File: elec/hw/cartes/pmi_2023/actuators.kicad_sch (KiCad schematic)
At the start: 43 parts, among them J1 con_servo, J2 con_servo, J3 con_servo, J4 con_servo, U23 PCA9685PW, U24 SN74LVC1T45DBV, U25 SN74LVC1T45DBV, U26 SN74LVC1T45DBV, U27 SN74LVC1T45DBV

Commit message: PAMI 2023: update jlc part number
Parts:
- R62, R63, R64: JLCPCB C2991540 -> C21190
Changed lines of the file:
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@@
 			)
 		)
-		(property "JLCPCB" "C2991540"
+		(property "JLCPCB" "C21190"
 			(at 166.37 33.02 0)
 			(effects
@@
 			)
 		)
-		(property "JLCPCB" "C2991540"
+		(property "JLCPCB" "C21190"
 			(at 149.86 33.02 0)
 			(effects
@@
 			)
 		)
-		(property "JLCPCB" "C2991540"
+		(property "JLCPCB" "C21190"
 			(at 137.16 33.02 0)
 			(effects

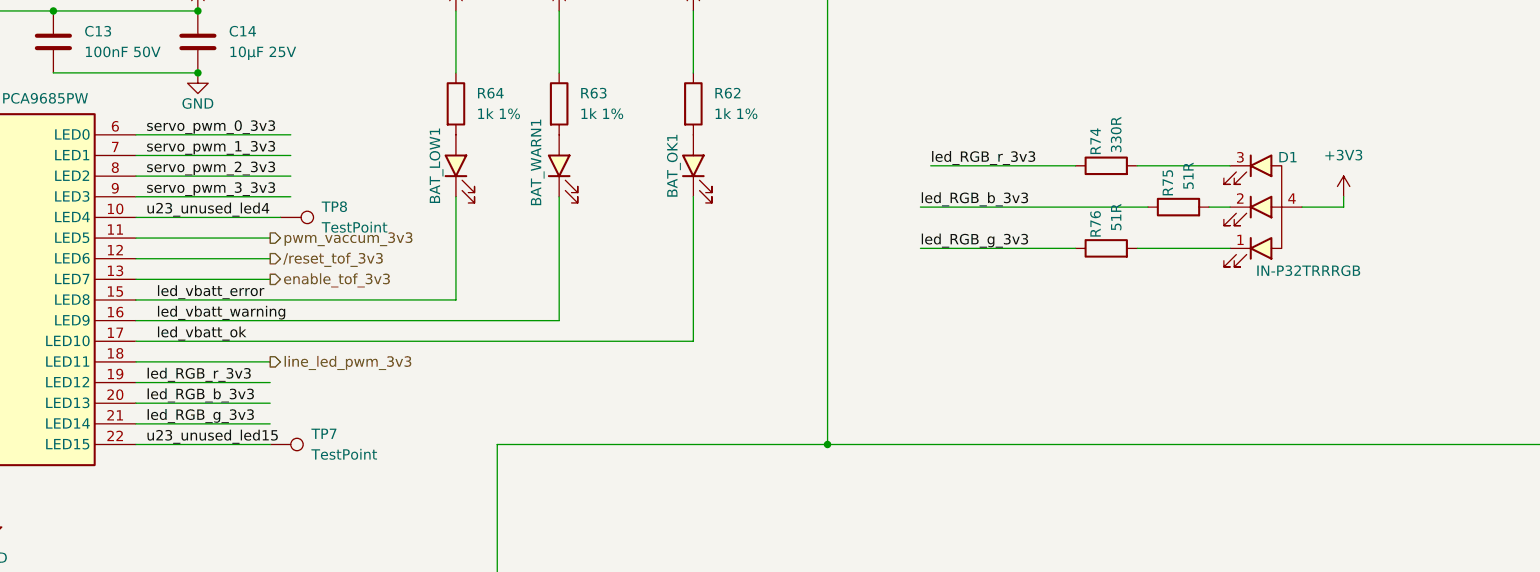
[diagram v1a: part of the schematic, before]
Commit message: GP2S60B replaced by ITR1204SR10A, RGB LED replaced by NH-B2020RGBA
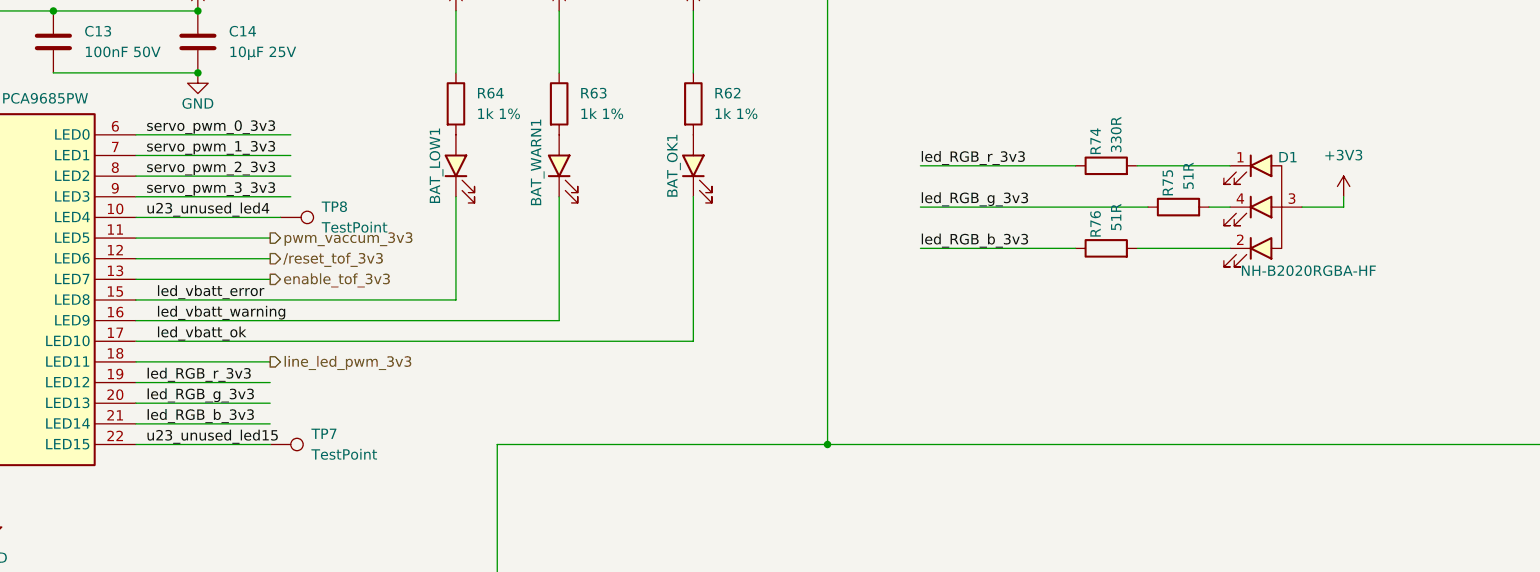
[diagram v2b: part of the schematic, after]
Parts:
- D1: value IN-P32TRRRGB -> NH-B2020RGBA-HF; footprint cocotter_diodes:3528_PLCC-Reverse_mount -> cocotter_diodes:NH-B2020RGBA-HF; symbol cocotter_diodes:IN-P32TRRRGB -> cocotter_diodes:NH-B2020RGBA-HF; JLCPCB C7288909 -> C2874116
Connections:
- net +3V3: now also D1.3 (COM); no longer D1.4 (COM)
- net led_RGB_b_3v3: now also R76.1, U23.21 (LED14); no longer R75.1, U23.20 (LED13)
- net led_RGB_g_3v3: now also R75.1, U23.20 (LED13); no longer R76.1, U23.21 (LED14)
- net at R75.2: now also D1.4 (C_GREEN); no longer D1.2 (C_GREEN)
- net at R76.2: now also D1.2 (C_BLUE); no longer D1.1 (C_BLUE)
- net at R74.2: now also D1.1 (C_RED); no longer D1.3 (C_RED)
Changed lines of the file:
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@@
 	(wire
 		(pts
-			(xy 195.58 40.64) (xy 213.36 40.64)
+			(xy 194.31 40.64) (xy 213.36 40.64)
 		)
 		(stroke
@@
 		)
 	)
-	(label "led_RGB_b_3v3"
+	(label "led_RGB_g_3v3"
 		(at 99.06 69.85 0)
 		(fields_autoplaced yes)
@@
 		)
 	)
-	(label "led_RGB_b_3v3"
+	(label "led_RGB_g_3v3"
 		(at 194.31 45.72 0)
 		(fields_autoplaced yes)
@@
 		)
 	)
-	(label "led_RGB_g_3v3"
+	(label "led_RGB_b_3v3"
 		(at 194.31 50.8 0)
 		(fields_autoplaced yes)
@@
 		)
 	)
-	(label "led_RGB_g_3v3"
+	(label "led_RGB_b_3v3"
 		(at 99.06 72.39 0)
 		(fields_autoplaced yes)
@@
 	)
 	(label "led_RGB_r_3v3"
-		(at 195.58 40.64 0)
+		(at 194.31 40.64 0)
 		(fields_autoplaced yes)
 		(effects
@@
 	)
 	(symbol
-		(lib_id "cocotter_diodes:IN-P32TRRRGB")
+		(lib_id "cocotter_diodes:NH-B2020RGBA-HF")
 		(at 237.49 45.72 0)
 		(unit 1)
@@
 			)
 		)
-		(property "Value" "IN-P32TRRRGB"
+		(property "Value" "NH-B2020RGBA-HF"
 			(at 242.062 53.594 0)
 			(effects
@@
 			)
 		)
-		(property "Footprint" "cocotter_diodes:3528_PLCC-Reverse_mount"
+		(property "Footprint" "cocotter_diodes:NH-B2020RGBA-HF"
 			(at 237.49 45.72 0)
 			(effects
@@
 			)
 		)
-		(property "Description" "RGB LED, reverse mount"
+		(property "Description" "RGB LED 2.1mm x 2.1mm"
 			(at 237.49 45.72 0)
 			(effects
@@
 			)
 		)
-		(property "JLCPCB" "C7288909"
+		(property "JLCPCB" "C2874116"
 			(at 237.49 45.72 0)
 			(effects

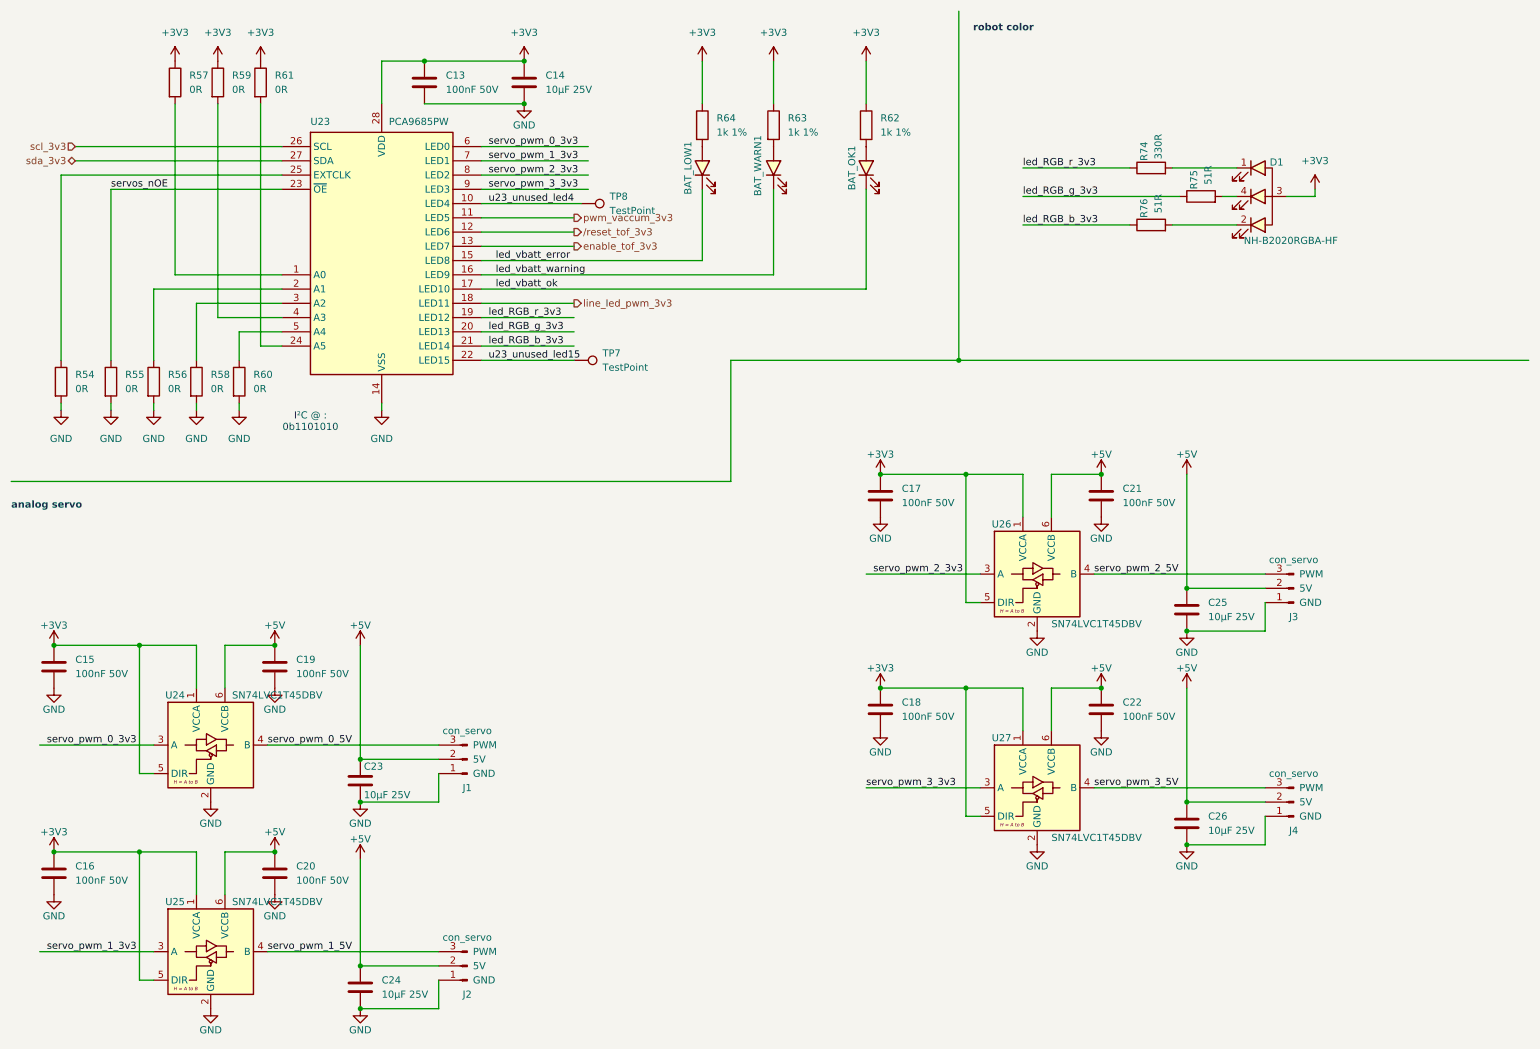
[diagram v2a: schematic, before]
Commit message: pmi_tof_sensor : last commit before tmf8821 deletion
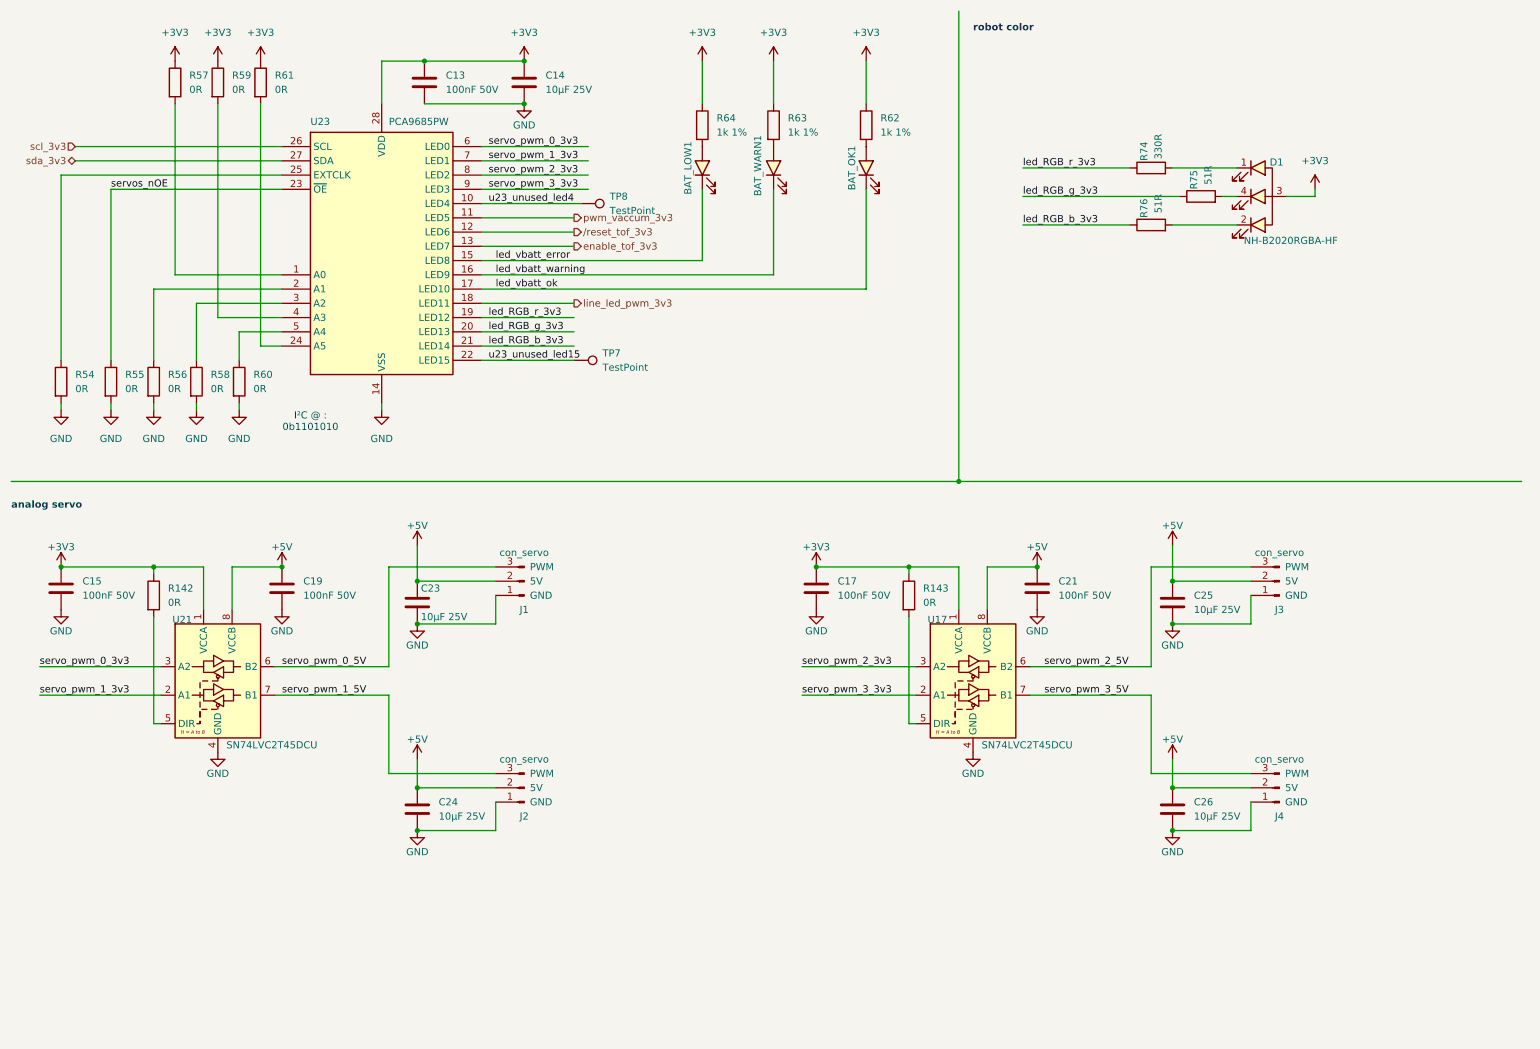
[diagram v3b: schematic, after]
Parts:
- removed C16, C18, C20, C22: 100nF 50V, cocotter_capacitors:C_0603_1608Metric, symbol cocotter_capacitors:C_100nF_50V_0603
- removed U24, U25, U26, U27: SN74LVC1T45DBV, Package_TO_SOT_SMD:SOT-23-6, symbol cocotter_ic:SN74LVC1T45DBV
- added R142, R143: 0R, cocotter_resistor:r0603_reflow, symbol cocotter_resistors:R_0R_0603
- added U17, U21: SN74LVC2T45DCU, cocotter_ic:VSSOP-8-DCU, symbol cocotter_ic:SN74LVC2T45DCU
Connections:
- net +3V3: now also R142.1, R143.1, U17.1 (VCCA), U21.1 (VCCA)
- net +5V: now also U17.8 (VCCB), U21.8 (VCCB)
- net GND: now also U17.4 (GND), U21.4 (GND)
- net servo_pwm_0_3v3: now also U21.3 (A2)
- net servo_pwm_0_5V: now also U21.6 (B2)
- net servo_pwm_1_3v3: now also U21.2 (A1)
- net servo_pwm_1_5V: now also U21.7 (B1)
- net servo_pwm_2_3v3: now also U17.3 (A2)
- net servo_pwm_2_5V: now also U17.6 (B2)
- net servo_pwm_3_3v3: now also U17.2 (A1)
- net servo_pwm_3_5V: now also U17.7 (B1)
- new net: R143.2, U17.5 (DIR)
- new net: R142.2, U21.5 (DIR)
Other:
- moved on the sheet: C15, C17, C19, C21, C23, C24, C25, C26, J1, J2, J3, J4

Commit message: XRA1200 replaced by TCA6408
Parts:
- BAT_LOW1: JLCPCB C2286 -> (none)
- BAT_OK1: JLCPCB C2290 -> (none); JLCPCB Part # (none) -> C2290
- BAT_WARN1: JLCPCB C2296 -> (none)
- C13, C15, C17, C19, C21: JLCPCB C14663 -> (none); JLCPCB Part # (none) -> C14663
- C14, C23, C24, C25, C26: JLCPCB C15850 -> (none); JLCPCB Part # (none) -> C15850
- D1: JLCPCB C2874116 -> (none); JLCPCB Part # (none) -> C2874116
- J1, J2, J3, J4: JLCPCB C2932698 -> (none); JLCPCB Part # (none) -> C2932698
- R142, R143, R54, R55, R56, R57, R58, R59, R60, R61: JLCPCB C431718 -> (none); JLCPCB Part # (none) -> C431718
- R62, R63, R64: JLCPCB C21190 -> (none); JLCPCB Part # (none) -> C2991540
- R74: JLCPCB C23138 -> (none); JLCPCB Part # (none) -> C23138
- R75, R76: JLCPCB C23197 -> (none); JLCPCB Part # (none) -> C23197
- U23: JLCPCB C2678753 -> (none); JLCPCB Part # (none) -> C2678753
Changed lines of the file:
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@@
 			)
 		)
-		(property "JLCPCB" "C2678753"
+		(property "JLCPCB Part #" "C2678753"
 			(at 80.01 54.61 0)
 			(effects
@@
 			)
 		)
-		(property "JLCPCB" "C431718"
+		(property "JLCPCB Part #" "C431718"
 			(at 173.99 116.84 0)
 			(effects
@@
 			)
 		)
-		(property "JLCPCB" "C14663"
+		(property "JLCPCB Part #" "C14663"
 			(at 62.23 115.57 0)
 			(effects
@@
 			)
 		)
-		(property "JLCPCB" "C15850"
+		(property "JLCPCB Part #" "C15850"
 			(at 86.36 118.11 0)
 			(effects
@@
 			)
 		)
-		(property "JLCPCB" "C15850"
+		(property "JLCPCB Part #" "C15850"
 			(at 220.98 154.94 0)
 			(effects
@@
 			)
 		)
-		(property "JLCPCB" "C21190"
+		(property "JLCPCB Part #" "C2991540"
 			(at 166.37 33.02 0)
 			(effects
@@
 			)
 		)
-		(property "JLCPCB" "C431718"
+		(property "JLCPCB Part #" "C431718"
 			(at 39.37 78.74 0)
 			(effects
@@
 			)
 		)
-		(property "JLCPCB" "C431718"
+		(property "JLCPCB Part #" "C431718"
 			(at 22.86 78.74 0)
 			(effects
@@
 			)
 		)
-		(property "JLCPCB" "C431718"
+		(property "JLCPCB Part #" "C431718"
 			(at 39.37 116.84 0)
 			(effects
@@
 			)
 		)
-		(property "JLCPCB" "C431718"
+		(property "JLCPCB Part #" "C431718"
 			(at 31.75 78.74 0)
 			(effects
@@
 			)
 		)
-		(property "JLCPCB" "C2932698"
+		(property "JLCPCB Part #" "C2932698"
 			(at 240.03 114.3 0)
 			(effects
@@
 			)
 		)
-		(property "JLCPCB" ""
+		(property "JLCPCB Part #" ""
 			(at 185.42 134.62 0)
 			(effects
@@
 			)
 		)
-		(property "JLCPCB" "C23197"
+		(property "JLCPCB Part #" "C23197"
 			(at 226.06 45.72 0)
 			(effects
@@
 			)
 		)
-		(property "JLCPCB" "C23197"
+		(property "JLCPCB Part #" "C23197"
 			(at 217.17 50.8 0)
 			(effects
@@
 			)
 		)
-		(property "JLCPCB" "C431718"
+		(property "JLCPCB Part #" "C431718"
 			(at 50.8 25.4 0)
 			(effects
@@
 			)
 		)
-		(property "JLCPCB" "C14663"
+		(property "JLCPCB Part #" "C14663"
 			(at 22.86 115.57 0)
 			(effects
@@
 			)
 		)
-		(property "JLCPCB" "C2932698"
+		(property "JLCPCB Part #" "C2932698"
 			(at 105.41 151.13 0)
 			(effects
@@
 			)
 		)
-		(property "JLCPCB" "C431718"
+		(property "JLCPCB Part #" "C431718"
 			(at 58.42 25.4 0)
 			(effects
@@
 			)
 		)
-		(property "JLCPCB" "C2932698"
+		(property "JLCPCB Part #" "C2932698"
 			(at 105.41 114.3 0)
 			(effects
@@
 			)
 		)
-		(property "JLCPCB" "C14663"
+		(property "JLCPCB Part #" "C14663"
 			(at 157.48 115.57 0)
 			(effects
@@
 			)
 		)
-		(property "JLCPCB" "C2286"
-			(at 137.16 40.64 0)
-			(effects
-				(font
-					(size 1.27 1.27)
-				)
-				(hide yes)
-			)
-		)
 		(pin "C"
 		)
@@
 			)
 		)
-		(property "JLCPCB" "C14663"
+		(property "JLCPCB Part #" "C14663"
 			(at 87.63 25.4 0)
 			(effects
@@
 			)
 		)
-		(property "JLCPCB" "C431718"
+		(property "JLCPCB Part #" "C431718"
 			(at 43.18 25.4 0)
 			(effects
@@
 			)
 		)
-		(property "JLCPCB" "C2296"
-			(at 149.86 40.64 0)
-			(effects
-				(font
-					(size 1.27 1.27)
-				)
-				(hide yes)
-			)
-		)
 		(pin "A"
 		)
@@
 			)
 		)
-		(property "JLCPCB" "C15850"
+		(property "JLCPCB Part #" "C15850"
 			(at 220.98 118.11 0)
 			(effects
@@
 			)
 		)
-		(property "JLCPCB" "C21190"
+		(property "JLCPCB Part #" "C2991540"
 			(at 149.86 33.02 0)
 			(effects
@@
 			)
 		)
-		(property "JLCPCB" "C2932698"
+		(property "JLCPCB Part #" "C2932698"
 			(at 240.03 151.13 0)
 			(effects
@@
 			)
 		)
-		(property "JLCPCB" "C14663"
+		(property "JLCPCB Part #" "C14663"
 			(at 196.85 115.57 0)
 			(effects
@@
 			)
 		)
-		(property "JLCPCB" "C15850"
+		(property "JLCPCB Part #" "C15850"
 			(at 86.36 154.94 0)
 			(effects
@@
 			)
 		)
-		(property "JLCPCB" ""
+		(property "JLCPCB Part #" ""
 			(at 50.8 134.62 0)
 			(effects
@@
 			)
 		)
-		(property "JLCPCB" "C15850"
+		(property "JLCPCB Part #" "C15850"
 			(at 105.41 25.4 0)
 			(effects
@@
 			)
 		)
-		(property "JLCPCB" "C23138"
+		(property "JLCPCB Part #" "C23138"
 			(at 217.17 40.64 0)
 			(effects
@@
 			)
 		)
-		(property "JLCPCB" "C431718"
+		(property "JLCPCB Part #" "C431718"
 			(at 54.61 78.74 0)
 			(effects
@@
 			)
 		)
-		(property "JLCPCB" "C431718"
+		(property "JLCPCB Part #" "C431718"
 			(at 46.99 78.74 0)
 			(effects
@@
 			)
 		)
-		(property "JLCPCB" "C2874116"
+		(property "JLCPCB Part #" "C2874116"
 			(at 237.49 45.72 0)
 			(effects
@@
 			)
 		)
-		(property "JLCPCB" "C2290"
+		(property "JLCPCB Part #" "C2290"
 			(at 166.37 40.64 0)
 			(effects
@@
 			)
 		)
-		(property "JLCPCB" "C21190"
+		(property "JLCPCB Part #" "C2991540"
 			(at 137.16 33.02 0)
 			(effects
